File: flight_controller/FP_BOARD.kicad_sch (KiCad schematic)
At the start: 0 parts

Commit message: gps and power blocks
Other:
- sheet POWER ports: added I2C1_SCL_INA226, I2C1_SDA_INA226; removed none
- sheet STM32H7 ports: added UART5_CTS_TELEM2, UART5_RTS_TELEM2, UART5_RX_TELEM2, UART5_TX_TELEM2, UART8_RX, UART8_TX, USART2_CTS_TELEM3, USART2_RTS_TELEM3, USART2_RX_TELEM3, USART2_TX_TELEM3; removed none
- sheet UART and GPS ports: added BUZZER_1, FMU_SAFETY_SWITCH_IN, FMU_nSAFETY_SWITCH_LED_OUT, I2C1_SCL_GPS1, I2C1_SDA_GPS1, IO_NSAFETY_SWITCH_LED_OUT, IO_SAFETY_SWITCH_IN, UART1_RX_GPS1, UART1_TX_GPS1, UART2_CTS_TELEM3, UART2_RTS_TELEM3, UART2_RX_TELEM3, UART2_TX_TELEM3, UART5_CTS_TELEM2, UART5_RTS_TELEM2, UART5_RX_TELEM2, UART5_TX_TELEM2, UART7_CTS_TELEM1, UART7_RTS_TELEM1, UART7_RX_TELEM1, UART7_TX_TELEM1, UART8_RX_GPS2, UART8_TX_GPS2; removed none

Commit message: ALL CONNECTORS, ETH, SERVO,RC,SPI,FLASH and more. to finish GPSand STM32 PINOUT
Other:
- sheet CAN and SPI bus renamed CAN and SPI
- sheet REVISIONS renamed SERVO_RC
- added sheet ETH (ETH.kicad_sch)
- sheet CAN and SPI ports: added SPI6_MISO, SPI6_MOSI, SPI6_SCK, SPI6_nCS1_EXTERNAL1, SPI6_nCS2_EXTERNAL1; removed none
- sheet SENSORS ports: added I2C3_SCL_EEPROM, I2C3_SDA_EEPROM, QUADSPI_BK1_IO0, QUADSPI_BK1_IO1, QUADSPI_BK1_IO2, QUADSPI_BK1_IO3, QUADSPI_BK1_NCS, QUADSPI_CLK; removed I2C2_DRDY1
- sheet SERVO_RC: file REVISIONS.kicad_sch -> SERVO_RC.kicad_sch
- sheet SERVO_RC ports: added IO_PPM_INPUT, IO_RSSI_IN, IO_SBUS_INPUT, IO_SBUS_OUTPUT, IO_USART1_RX_DSM, NSBUS_OUT_EN; removed none
- sheet STM32F1 ports: added none; removed STM32F1_NRST
- sheet STM32H7 ports: added ETH_CRS_DV, ETH_MDC, ETH_MDIO, ETH_REF_CLK, ETH_RXD0, ETH_RXD1, ETH_TXD0, ETH_TXD1, ETH_TX_EN, I2C3_SCL, I2C3_SDA, QUADSPI_BK1_IO0, QUADSPI_BK1_IO1, QUADSPI_BK1_IO2, QUADSPI_BK1_IO3, QUADSPI_BK1_NCS, QUADSPI_CLK, SPI6_MISO, SPI6_MOSI, SPI6_SCK, SPI6_nCS1_EXTERNAL1, SPI6_nCS2_EXTERNAL1, UART4_RX, UART4_TX; removed FMU_CH5, I2C2_DRDY1
- sheet UART and GPS: file UART and GPS.kicad_sch -> UART_GPS.kicad_sch
- sheet UART and GPS ports: added I2C2_SCL_GPS2, I2C2_SDA_GPS2, I2C3_SCL, I2C3_SDA, UART4_RX, UART4_TX; removed none

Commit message: cleanup and improvements
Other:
- sheet UART and GPS renamed TELEM
- added sheet GPS (GPS.kicad_sch)
- sheet CAN and SPI ports: added SPI3_MISO, SPI3_MOSI, SPI3_SCK, SPI3_nCS1; removed SPI6_MISO, SPI6_MOSI, SPI6_SCK, SPI6_nCS1_EXTERNAL1, SPI6_nCS2_EXTERNAL1
- sheet SENSORS ports: added SD_CARD_DETECT; removed none
- sheet SERVO_RC ports: added none; removed FMU_CH5, FMU_CH7, FMU_CH8, IO_CH6, IO_CH7, IO_CH8
- sheet STM32F1 ports: added IO_USART1_RX_DSM_VCP; removed IO_CH6, IO_CH7, IO_CH8, IO_USART1_RX_DSM
- sheet STM32H7 ports: added SD_CARD_DETECT, SPI3_MISO, SPI3_MOSI, SPI3_SCK, SPI3_nCS1; removed FMU_CH7, FMU_CH8, SPI6_MISO, SPI6_MOSI, SPI6_SCK, SPI6_nCS1_EXTERNAL1, SPI6_nCS2_EXTERNAL1, VDD_3V3_SPEKTRUM_POWER_EN, VDD_5V_HIPOWER_nEN, VDD_5V_HIPOWER_nOC, VDD_5V_PERIPH_nEN, VDD_5V_PERIPH_nOC, nPOWER_IN_A, nPOWER_IN_B, nPOWER_IN_C
- sheet TELEM: file UART_GPS.kicad_sch -> TELEM.kicad_sch
- sheet TELEM ports: added none; removed BUZZER_1, FMU_SAFETY_SWITCH_IN, FMU_nSAFETY_SWITCH_LED_OUT, I2C1_SCL_GPS1, I2C1_SDA_GPS1, I2C2_SCL_GPS2, I2C2_SDA_GPS2, IO_NSAFETY_SWITCH_LED_OUT, IO_SAFETY_SWITCH_IN, UART1_RX_GPS1, UART1_TX_GPS1, UART8_RX_GPS2, UART8_TX_GPS2

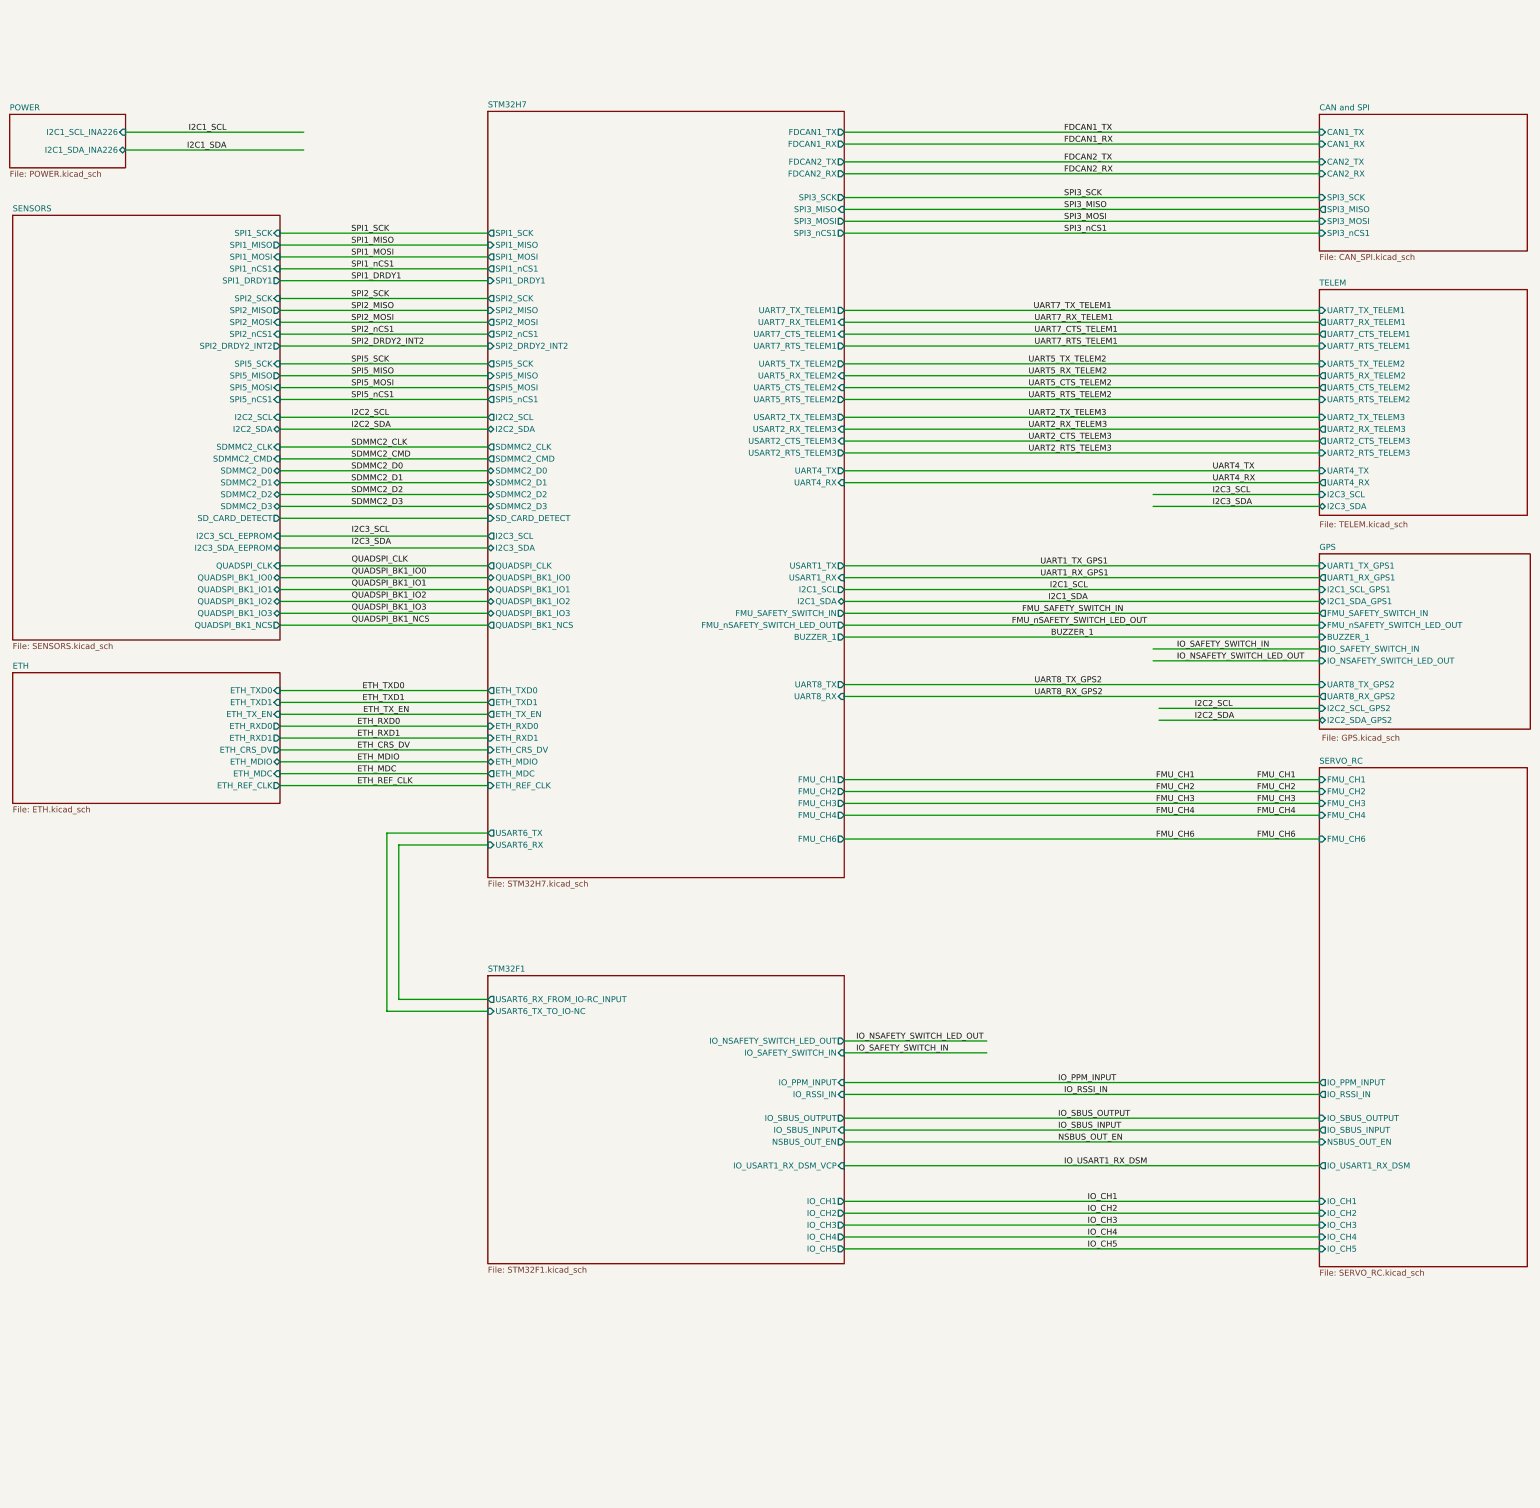
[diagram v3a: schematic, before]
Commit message: Schematic complete, ready for layout. Added USB, TPs, power conn, updated clocks, ran Rules Checker and general review
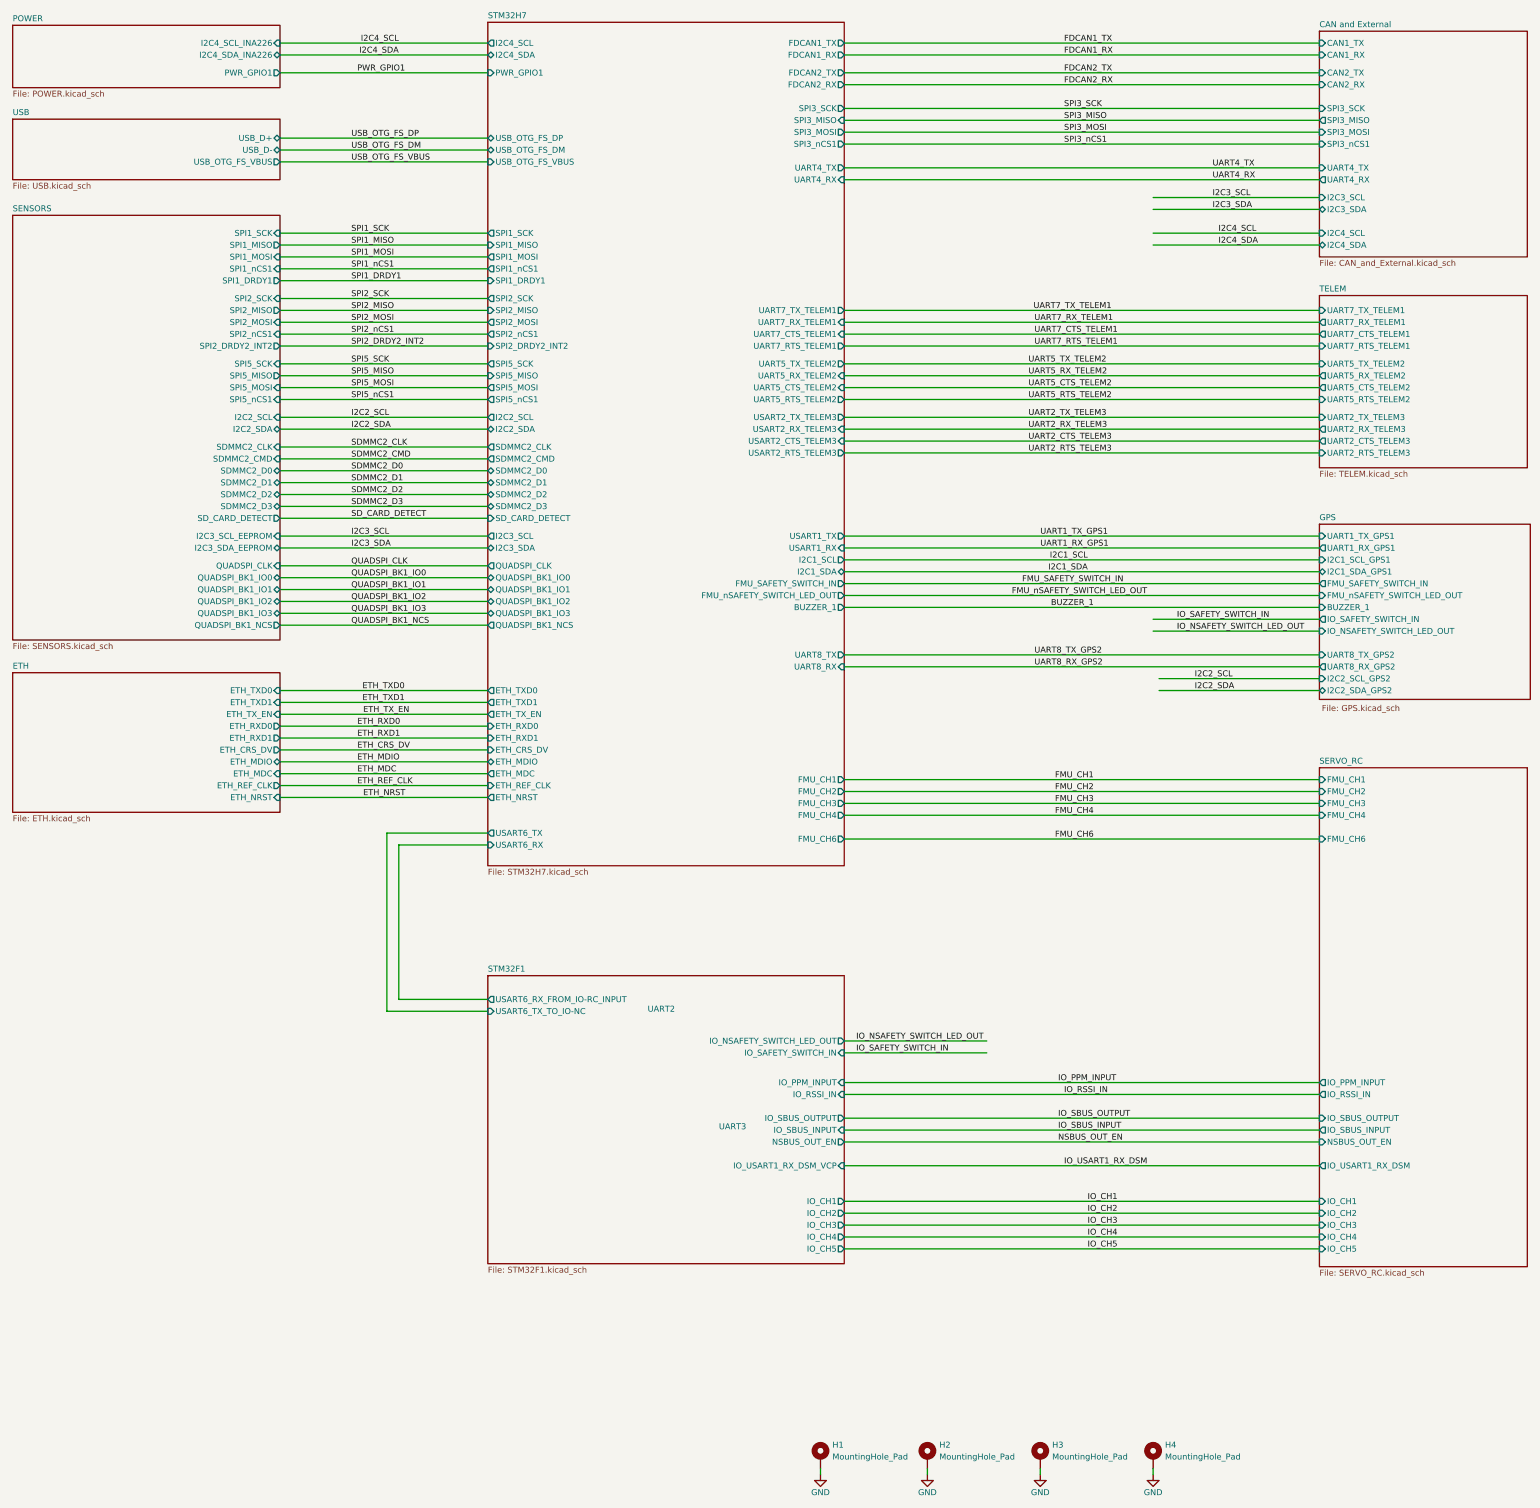
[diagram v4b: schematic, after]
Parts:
- added H1, H2, H3, H4: MountingHole_Pad, MountingHole:MountingHole_2.2mm_M2_Pad, symbol Mechanical:MountingHole_Pad
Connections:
- new net GND: H1.1, H2.1, H3.1, H4.1
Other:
- sheet CAN and SPI renamed CAN and External
- added sheet USB (USB.kicad_sch)
- sheet CAN and External: file CAN_SPI.kicad_sch -> CAN_and_External.kicad_sch
- sheet CAN and External ports: added I2C3_SCL, I2C3_SDA, I2C4_SCL, I2C4_SDA, UART4_RX, UART4_TX; removed none
- sheet ETH ports: added ETH_NRST; removed none
- sheet POWER ports: added I2C4_SCL_INA226, I2C4_SDA_INA226, PWR_GPIO1; removed I2C1_SCL_INA226, I2C1_SDA_INA226
- sheet STM32H7 ports: added ETH_NRST, I2C4_SCL, I2C4_SDA, PWR_GPIO1, USB_OTG_FS_DM, USB_OTG_FS_DP, USB_OTG_FS_VBUS; removed none
- sheet TELEM ports: added none; removed I2C3_SCL, I2C3_SDA, UART4_RX, UART4_TX
- note added: "UART2"
- note added: "UART3"

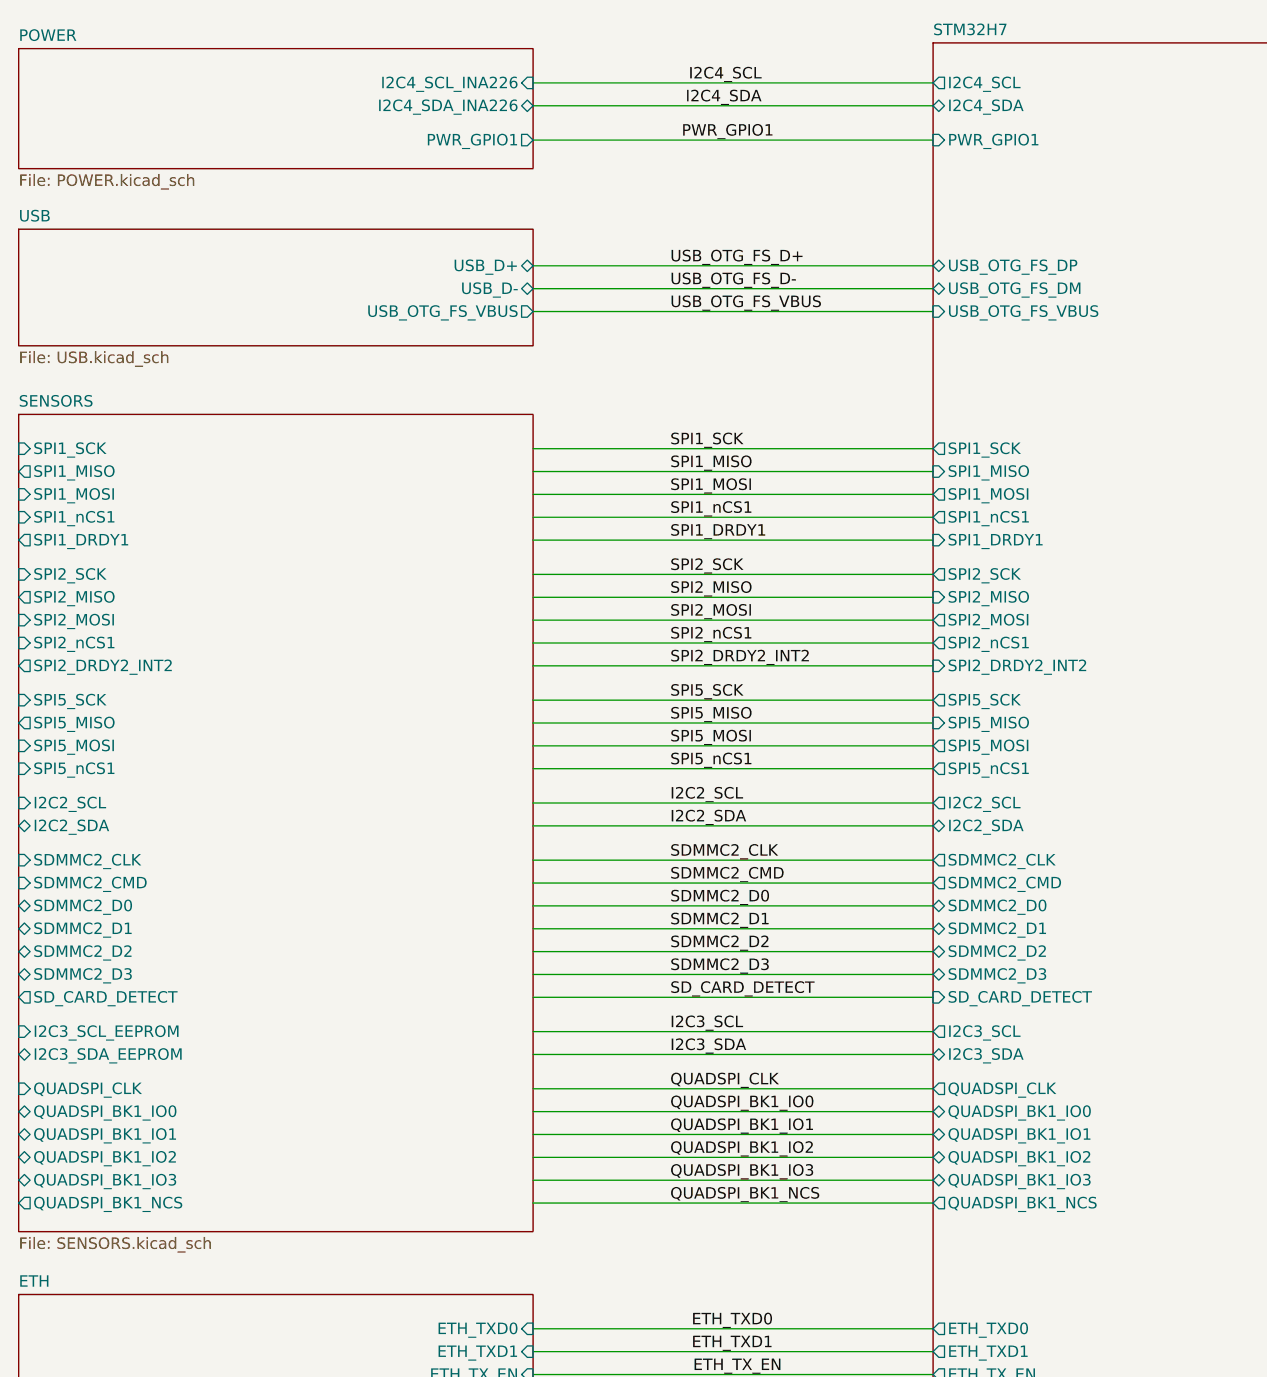
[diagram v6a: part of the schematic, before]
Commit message: Updated power and usb connectors, annotations and netlist check
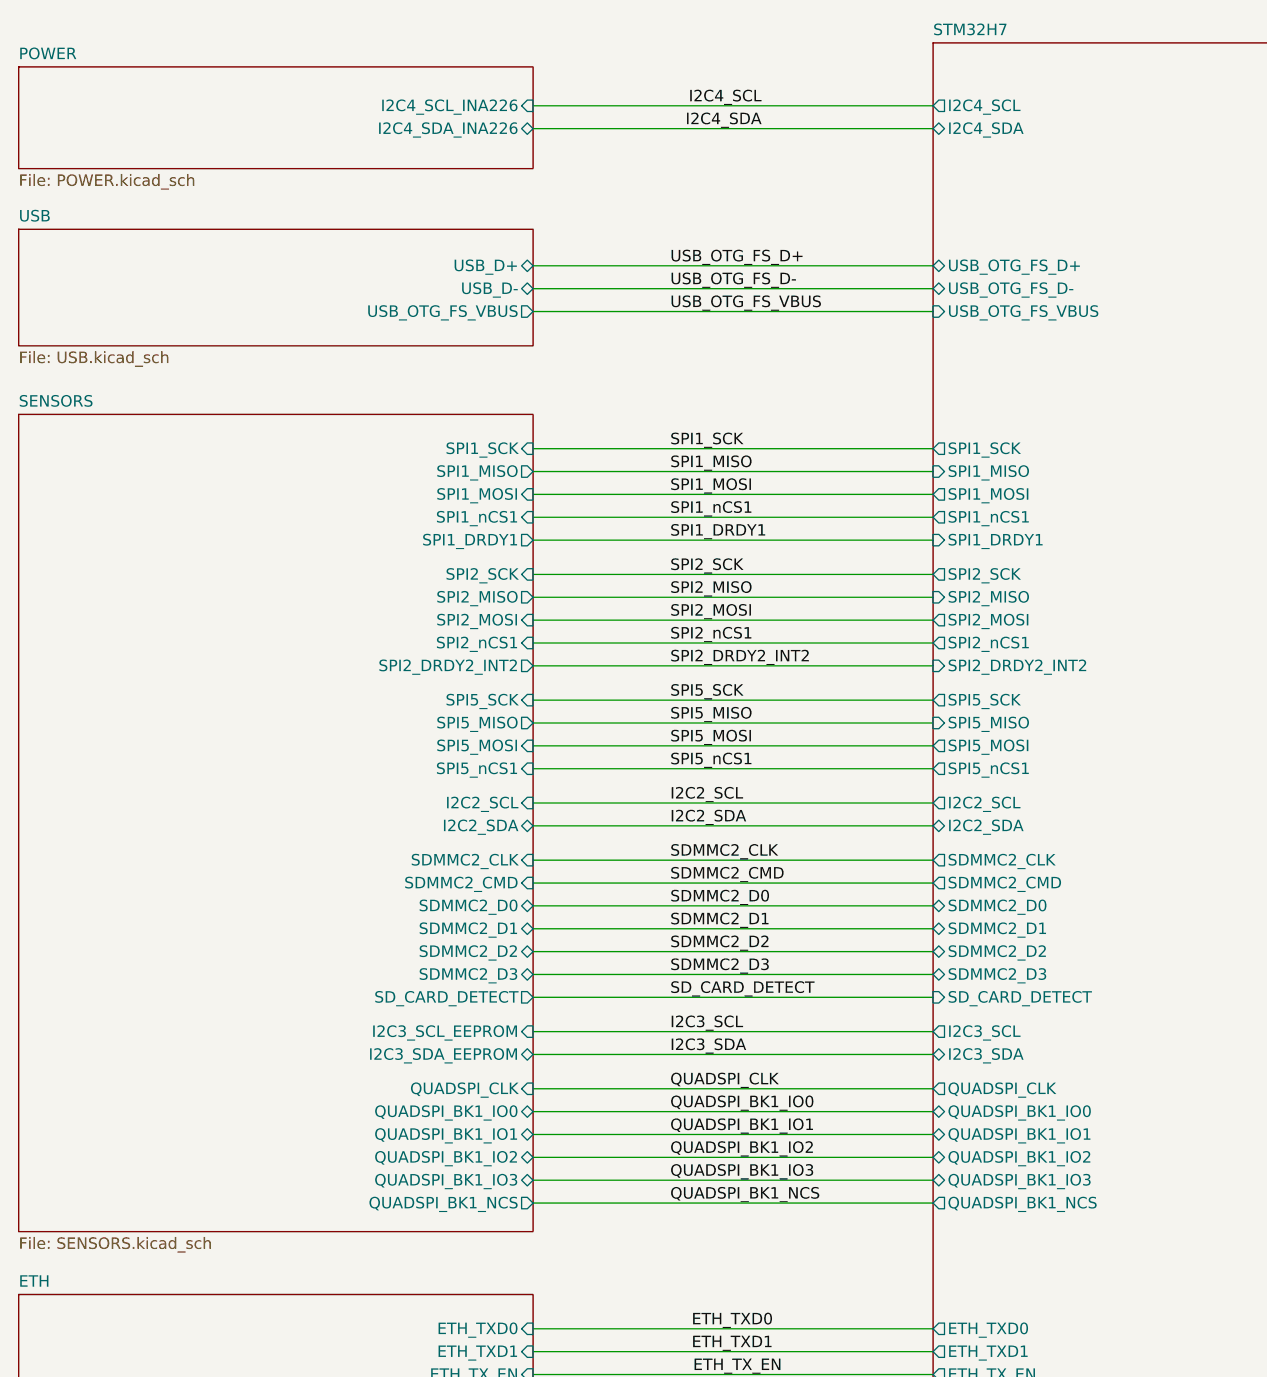
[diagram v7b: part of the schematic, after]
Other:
- sheet POWER ports: added none; removed PWR_GPIO1
- sheet STM32H7 ports: added USB_OTG_FS_D+, USB_OTG_FS_D-; removed PWR_GPIO1, USB_OTG_FS_DM, USB_OTG_FS_DP
